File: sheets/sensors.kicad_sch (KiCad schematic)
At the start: 13 parts, among them CN1 StemmaQT, U6 SparkfunM9N, U7 BMP581, U8 ADXL345BCCZ-RL7, U9 ADXL375BCCZ-RL7

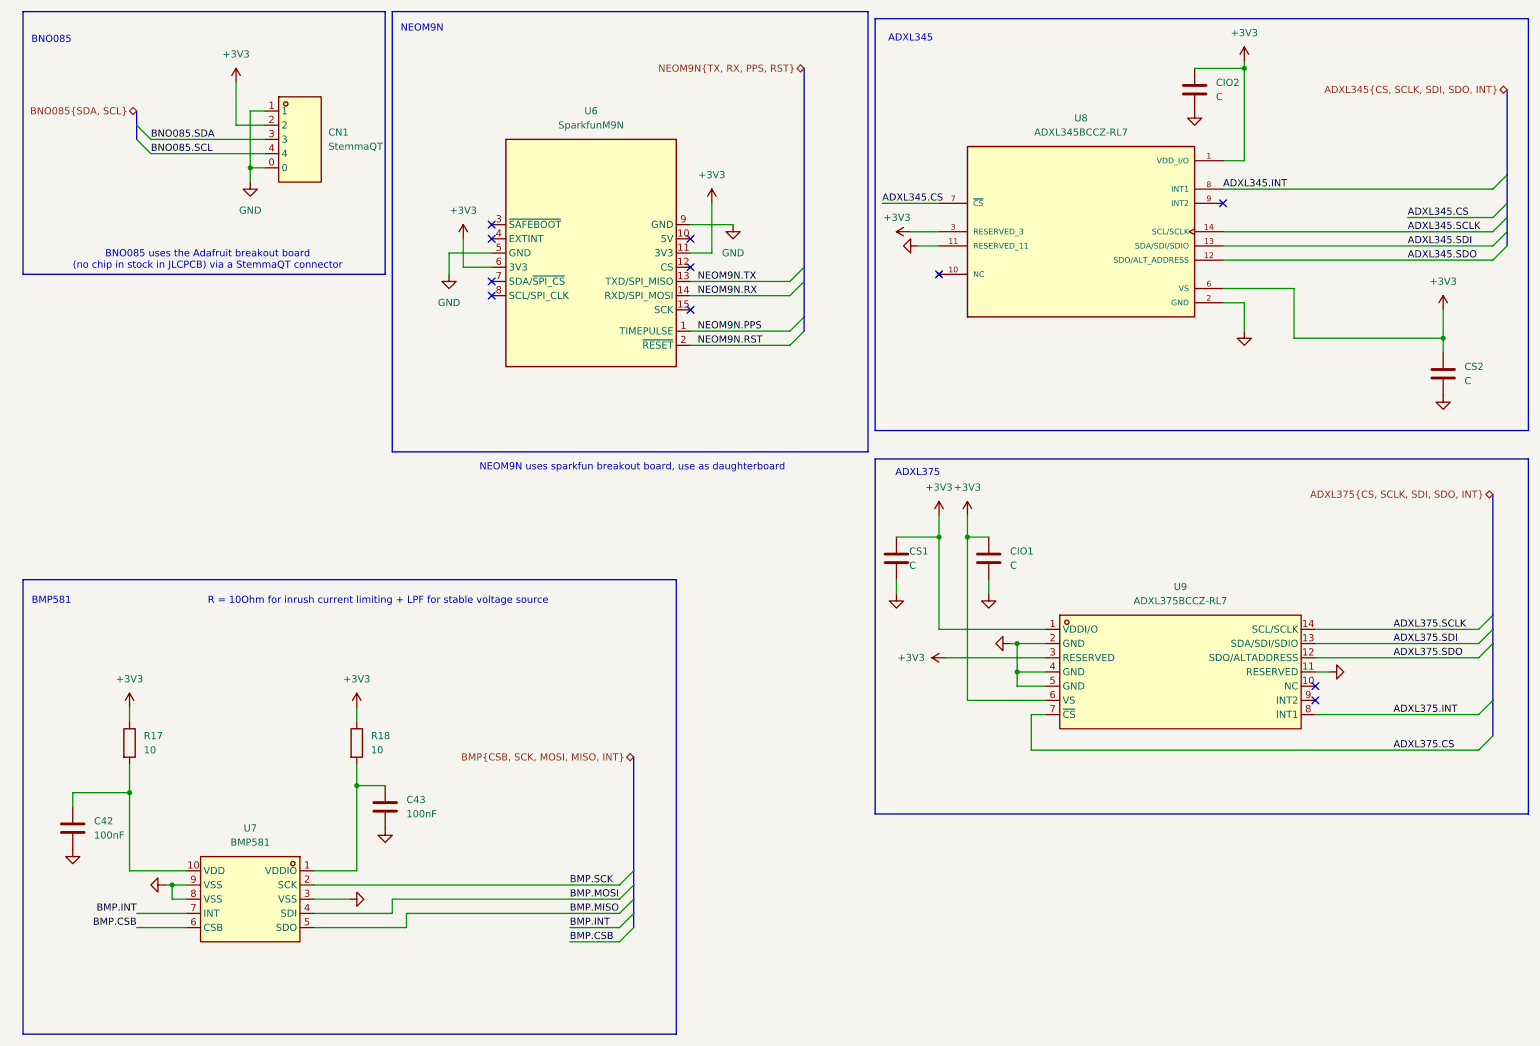
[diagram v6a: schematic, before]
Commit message: Cleared ALL ERC warnings
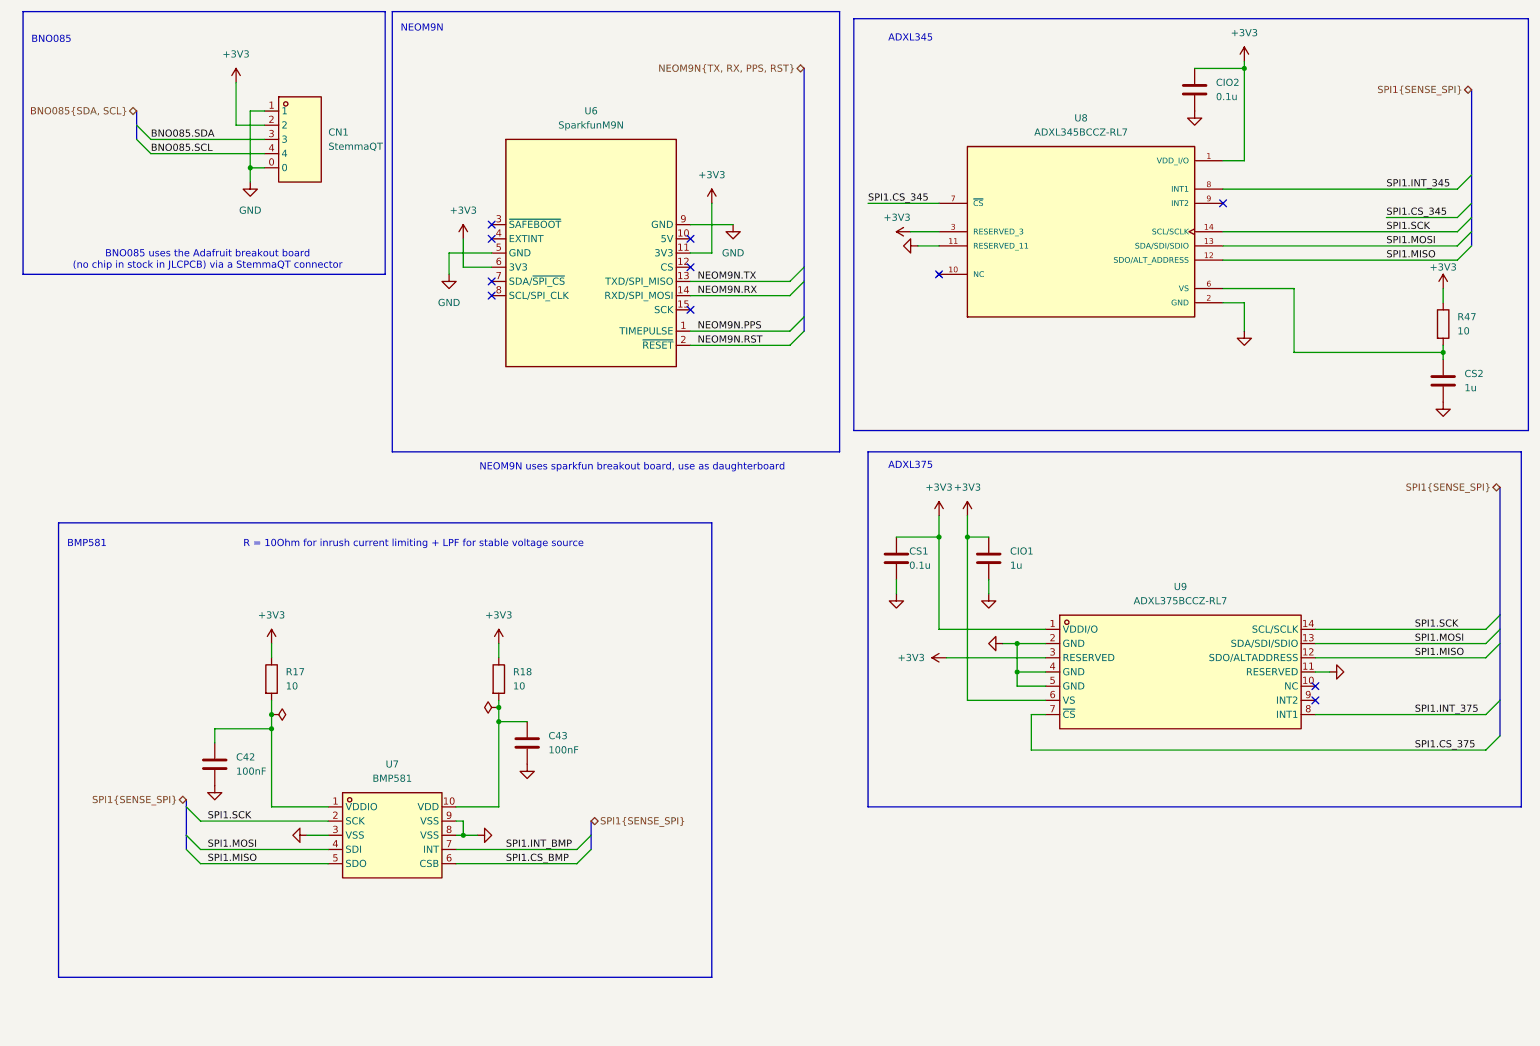
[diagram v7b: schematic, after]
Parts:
- added R47: 10, symbol Device:R
- CIO1, CS2: value C -> 1u
- CIO2, CS1: value C -> 0.1u
- U6: footprint aerolotl_custom:SparkfunM9N -> RF_GPS:ublox_NEO
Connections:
- net ADXL375.SCLK is gone; now on net SPI1.SCK: U9.14 (SCL/SCLK)
- net ADXL375.SDI is gone; now on net SPI1.MOSI: U9.13 (SDA/SDI/SDIO)
- net ADXL375.SDO is gone; now on net SPI1.MISO: U9.12 (SDO/ALTADDRESS)
- net BMP.MISO is gone; now on net SPI1.MISO: U7.5 (SDO)
- net BMP.MOSI is gone; now on net SPI1.MOSI: U7.4 (SDI)
- net BMP.SCK is gone; now on net SPI1.SCK: U7.2 (SCK)
- net +3V3: now also R47.1; no longer CS2.1, U8.6 (VS)
- net at C42.1, R17.2: now also U7.1 (VDDIO); no longer U7.10 (VDD)
- net at C43.1, R18.2: now also U7.10 (VDD); no longer U7.1 (VDDIO)
- net ADXL345.CS renamed SPI1.CS_345
- net ADXL345.INT renamed SPI1.INT_345
- net ADXL345.SCLK renamed SPI1.SCK
- net ADXL345.SDI renamed SPI1.MOSI
- net ADXL345.SDO renamed SPI1.MISO
- net ADXL375.CS renamed SPI1.CS_375
- net ADXL375.INT renamed SPI1.INT_375
- net BMP.CSB renamed SPI1.CS_BMP
- net BMP.INT renamed SPI1.INT_BMP
- new net: CS2.1, R47.2, U8.6 (VS)
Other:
- moved on the sheet: C42, C43, CS2, R17, R18

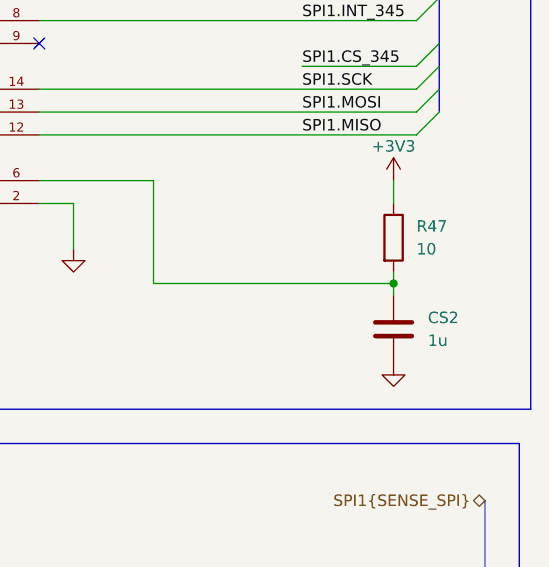
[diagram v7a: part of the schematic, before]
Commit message: added capacitor values to sensors
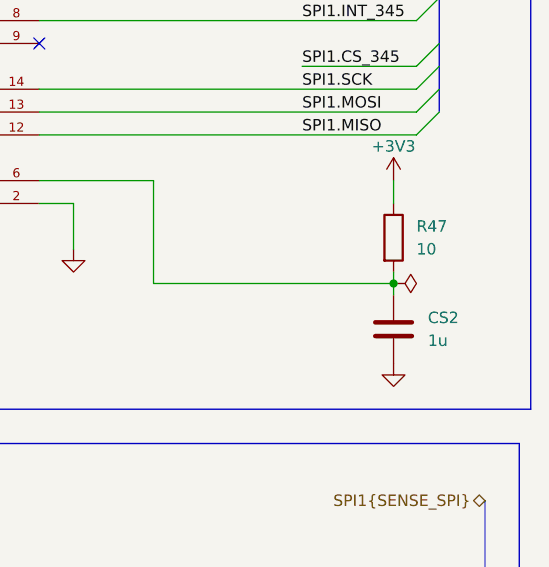
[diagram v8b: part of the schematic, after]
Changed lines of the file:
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@@
+		)
+	)
+	(symbol
+		(lib_id "power:PWR_FLAG")
+		(at 267.97 74.93 270)
+		(unit 1)
+		(exclude_from_sim no)
+		(in_bom yes)
+		(on_board yes)
+		(dnp no)
+		(fields_autoplaced yes)
+		(property "Reference" "#FLG011"
+			(at 269.875 74.93 0)
+			(effects
+				(font
+					(size 1.27 1.27)
+				)
+				(hide yes)
+			)
+		)
+		(property "Value" "PWR_FLAG"
+			(at 273.05 74.93 0)
+			(effects
+				(font
+					(size 1.27 1.27)
+				)
+				(hide yes)
+			)
+		)
+		(property "Footprint" ""
+			(at 267.97 74.93 0)
+			(effects
+				(font
+					(size 1.27 1.27)
+				)
+				(hide yes)
+			)
+		)
+		(property "Datasheet" "~"
+			(at 267.97 74.93 0)
+			(effects
+				(font
+					(size 1.27 1.27)
+				)
+				(hide yes)
+			)
+		)
+		(property "Description" "Special symbol for telling ERC where power comes from"
+			(at 267.97 74.93 0)
+			(effects
+				(font
+					(size 1.27 1.27)
+				)
+				(hide yes)
+			)
+		)
+		(pin "1"
+		)
+		(instances
+			(project ""
+				(path "/3f5bc5ea-feaa-4ed9-b0e0-c918b1fb5754/74e9b1e9-3a21-4de4-9795-bce3dd5092b3"
+					(reference "#FLG011")
+					(unit 1)
+				)
+			)
 		)
 	)
